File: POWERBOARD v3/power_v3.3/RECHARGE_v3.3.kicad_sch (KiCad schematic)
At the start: 27 parts, among them J1 43650-0300, J2 UJ20-C-H-G-SMT-1-P16-TR, U1 USBLC6-2, U2 BQ25886RGE

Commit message: Removed NTC from TS node
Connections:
- net NTC: no longer R6.1, R7.2, U2.7 (TS)
- new net TS: R6.1, R7.2, U2.7 (TS)
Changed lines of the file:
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@@
-	)
-	(junction
-		(at 209.55 46.99)
-		(diameter 0)
-		(color 0 0 0 0)
 	)
 	(junction
@@
 		(pts
 			(xy 237.49 107.95) (xy 229.87 107.95)
-		)
-		(stroke
-			(width 0)
-			(type default)
-		)
-	)
-	(wire
-		(pts
-			(xy 209.55 46.99) (xy 217.17 46.99)
 		)
 		(stroke
@@
 			(hide yes)
 			(show_name no)
-			(do_not_autoplace no)
-			(effects
-				(font
-					(size 1.27 1.27)
-				)
-				(justify left)
-			)
-		)
-	)
-	(global_label "NTC"
-		(shape bidirectional)
-		(at 217.17 46.99 0)
-		(fields_autoplaced yes)
-		(effects
-			(font
-				(size 1.27 1.27)
-			)
-			(justify left)
-		)
-		(property "Intersheetrefs" "${INTERSHEET_REFS}"
-			(at 224.8346 46.99 0)
-			(hide yes)
-			(show_name no)

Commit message: Changed S1 pin 1 from no connect to passive, connected to gnd on layout to follow schematic
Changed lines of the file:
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@@
 	)
 	(junction
+		(at 71.12 110.49)
+		(diameter 0)
+		(color 0 0 0 0)
+	)
+	(junction
 		(at 54.61 54.61)
 		(diameter 0)
@@
 	(wire
 		(pts
-			(xy 49.53 110.49) (xy 78.74 110.49)
+			(xy 49.53 110.49) (xy 71.12 110.49)
 		)
 		(stroke
@@
 	(wire
 		(pts
+			(xy 71.12 110.49) (xy 78.74 110.49)
+		)
+		(stroke
+			(width 0)
+			(type default)
+		)
+	)
+	(wire
+		(pts
 			(xy 58.42 154.94) (xy 66.04 154.94)
 		)
@@
 					(unit 1)
 				)
+			)
+		)
+	)
+	(symbol
+		(lib_id "power:PWR_FLAG")
+		(at 71.12 110.49 180)
+		(unit 1)
+		(body_style 1)
+		(exclude_from_sim no)
+		(in_bom yes)
+		(on_board yes)
+		(in_pos_files yes)
+		(dnp no)
+		(fields_autoplaced yes)
+		(property "Reference" "#FLG01"
+			(at 71.12 112.395 0)
+			(hide yes)
+			(show_name no)
+			(do_not_autoplace no)
+			(effects
+				(font
+					(size 1.27 1.27)
+				)
+			)
+		)
+		(property "Value" "PWR_FLAG"
+			(at 71.12 115.57 0)
+			(show_name no)
+			(do_not_autoplace no)
+			(effects
+				(font
+					(size 1.27 1.27)
+				)
+			)
+		)
+		(property "Footprint" ""
+			(at 71.12 110.49 0)
+			(hide yes)
+			(show_name no)
+			(do_not_autoplace no)
+			(effects
+				(font
+					(size 1.27 1.27)
+				)
+			)
+		)
+		(property "Datasheet" ""
+			(at 71.12 110.49 0)
+			(hide yes)
+			(show_name no)
+			(do_not_autoplace no)
+			(effects
+				(font
+					(size 1.27 1.27)
+				)
+			)
+		)
+		(property "Description" "Special symbol for telling ERC where power comes from"
+			(at 71.12 110.49 0)
+			(hide yes)
+			(show_name no)
+			(do_not_autoplace no)
+			(effects
+				(font
+					(size 1.27 1.27)
+				)
+			)
+		)
+		(pin "1"
+		)
+		(instances
+			(project "power_v3.3"
+				(path "/432bcdcf-747a-4fa0-b87b-096f44260199/ef6b3a2b-31e3-4ffb-9457-e6034dbdb4b5"
+					(reference "#FLG01")
+					(unit 1)
+				)

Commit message: Made BOM with Customer PNs
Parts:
- BAT1: Added to order (none) -> NA; Customer PN (none) -> NA
- C1, C4: Added to order (none) -> Y; Customer PN (none) -> EMG-PWR-040A
- C13, C2: Added to order (none) -> Y; Customer PN (none) -> EMG-PWR-038
- C3: Added to order (none) -> Y; Customer PN (none) -> EMG-PWR-037
- C5: Added to order (none) -> Y; Customer PN (none) -> EMG-PWR-036
- C6, C7, C8: Added to order (none) -> Y; Customer PN (none) -> EMG-PWR-040B
- D1, D2: Added to order (none) -> Y; Customer PN (none) -> EMG-PWR-033
- D6: Added to order (none) -> Y; Customer PN (none) -> EMG-PWR-009
- J1: Added to order (none) -> Y; Customer PN (none) -> EMG-PWR-005
- J2: Added to order (none) -> Y; Customer PN (none) -> EMG-PWR-011
- L1: Added to order (none) -> Y; Customer PN (none) -> EMG-PWR-041
- R1: Added to order (none) -> Y; Customer PN (none) -> EMG-PWR-031
- R2: Added to order (none) -> Y; Customer PN (none) -> EMG-PWR-030
- R3, R5: Added to order (none) -> Y; Customer PN (none) -> EMG-PWR-029
- R4: Added to order (none) -> Y; Customer PN (none) -> EMG-PWR-028
- R6: Added to order (none) -> Y; Customer PN (none) -> EMG-PWR-027
- R7: Added to order (none) -> Y; Customer PN (none) -> EMG-PWR-026
- R8, R9: Added to order (none) -> Y; Customer PN (none) -> EMG-PWR-025
- U1: Added to order (none) -> Y; Customer PN (none) -> EMG-PWR-010
- U2: Added to order (none) -> Y; Customer PN (none) -> EMG-PWR-018

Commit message: Added test point footprints
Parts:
- BAT1: Added to order NA -> (none); Customer PN NA -> EMG-PWR-042
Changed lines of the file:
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@@
 			)
 		)
-		(property "Added to order" "NA"
+		(property "Added to order" ""
 			(at 231.14 130.81 0)
 			(hide yes)
@@
 			)
 		)
-		(property "Customer PN" "NA"
+		(property "Customer PN" "EMG-PWR-042"
 			(at 231.14 130.81 0)
 			(hide yes)

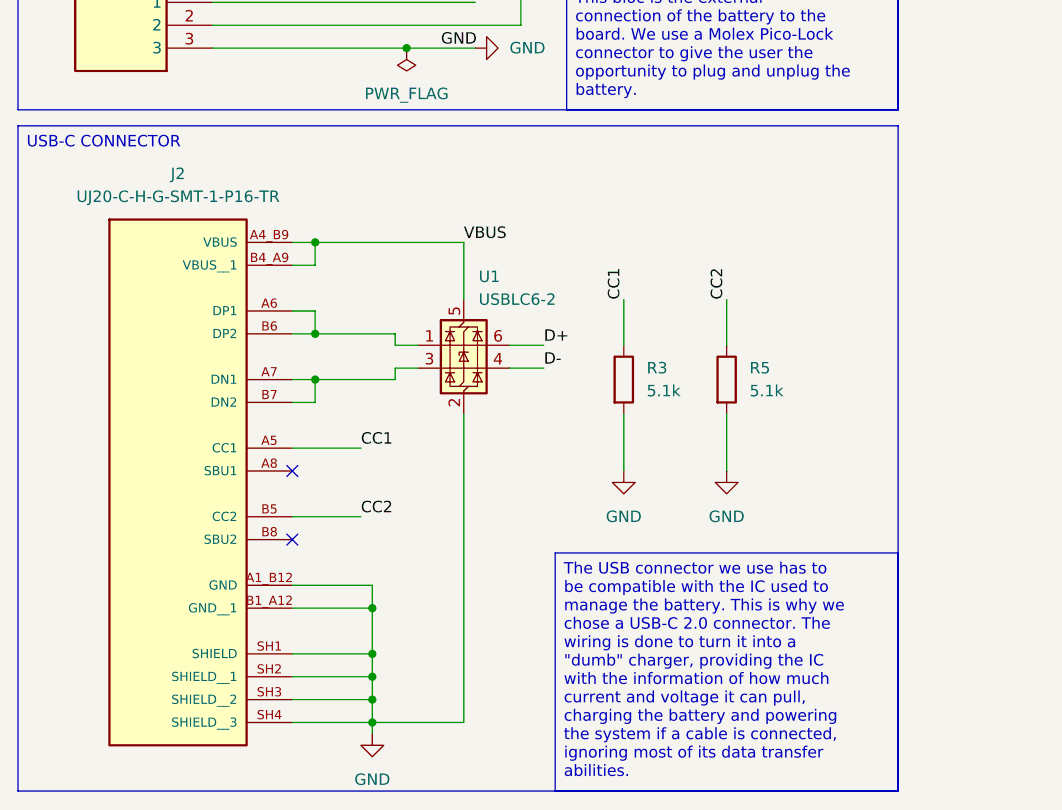
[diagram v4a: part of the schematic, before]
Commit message: Changed USB-C schematic to new connector symbol
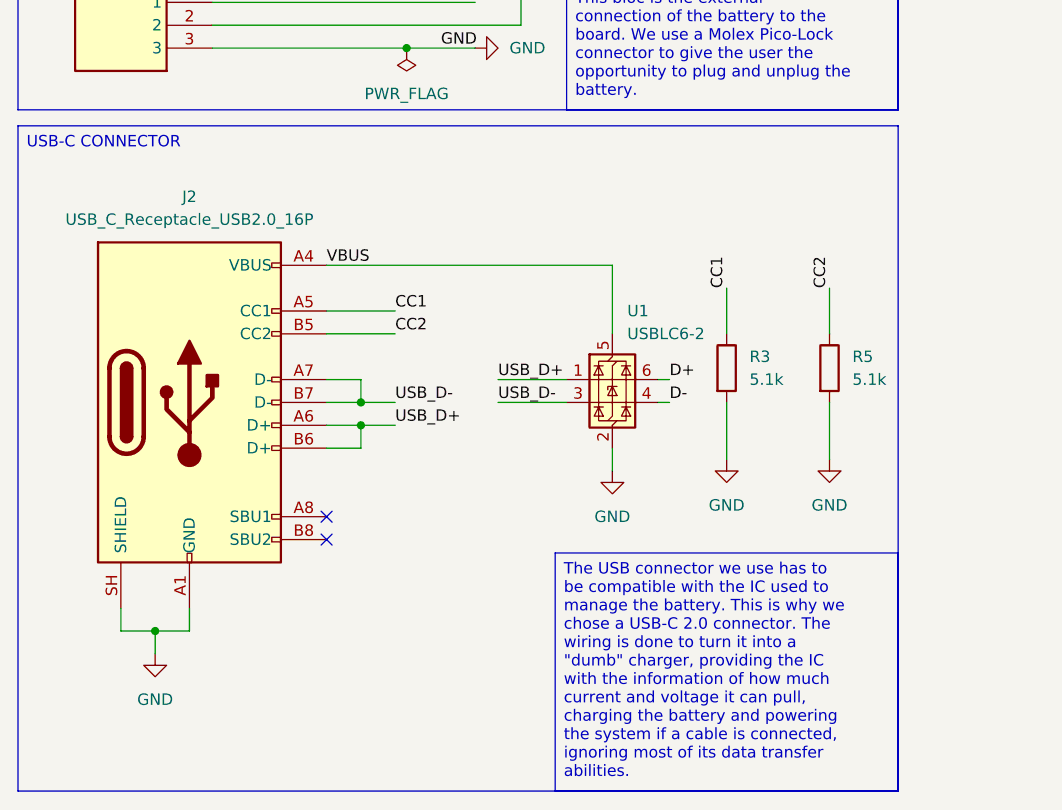
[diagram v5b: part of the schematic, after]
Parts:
- removed J2: UJ20-C-H-G-SMT-1-P16-TR, UJ20_C_H_G_SMT_1_P16_TR:SAMESKY_UJ20-C-H-G-SMT-1-P16-TR, symbol UJ20-C-H-G-SMT-1-P16-TR:UJ20-C-H-G-SMT-1-P16-TR
- added J2: USB_C_Receptacle_USB2.0_16P, Connector_USB:USB_C_Receptacle_GCT_USB4110, symbol Connector:USB_C_Receptacle_USB2.0_16P
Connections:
- net CC1: now also J2.A5 (CC1)
- net CC2: now also J2.B5 (CC2)
- net GND: now also J2.A1 (GND), J2.A12 (GND), J2.B1 (GND), J2.B12 (GND), J2.SH (SHIELD)
- net VBUS: now also J2.A4 (VBUS), J2.A9 (VBUS), J2.B4 (VBUS), J2.B9 (VBUS)
- net USB_D+: now reaches U1.1 (I/O1)
- net USB_D+: now also J2.A6 (D+), J2.B6 (D+)
- net USB_D-: now reaches U1.3 (I/O2)
- net USB_D-: now also J2.A7 (D-), J2.B7 (D-)
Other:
- moved on the sheet: R3, R5
